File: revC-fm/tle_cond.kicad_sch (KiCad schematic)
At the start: 13 parts, among them U33 AD1585ARTZ-REEL7, U34 LT6004CMS8#PBF

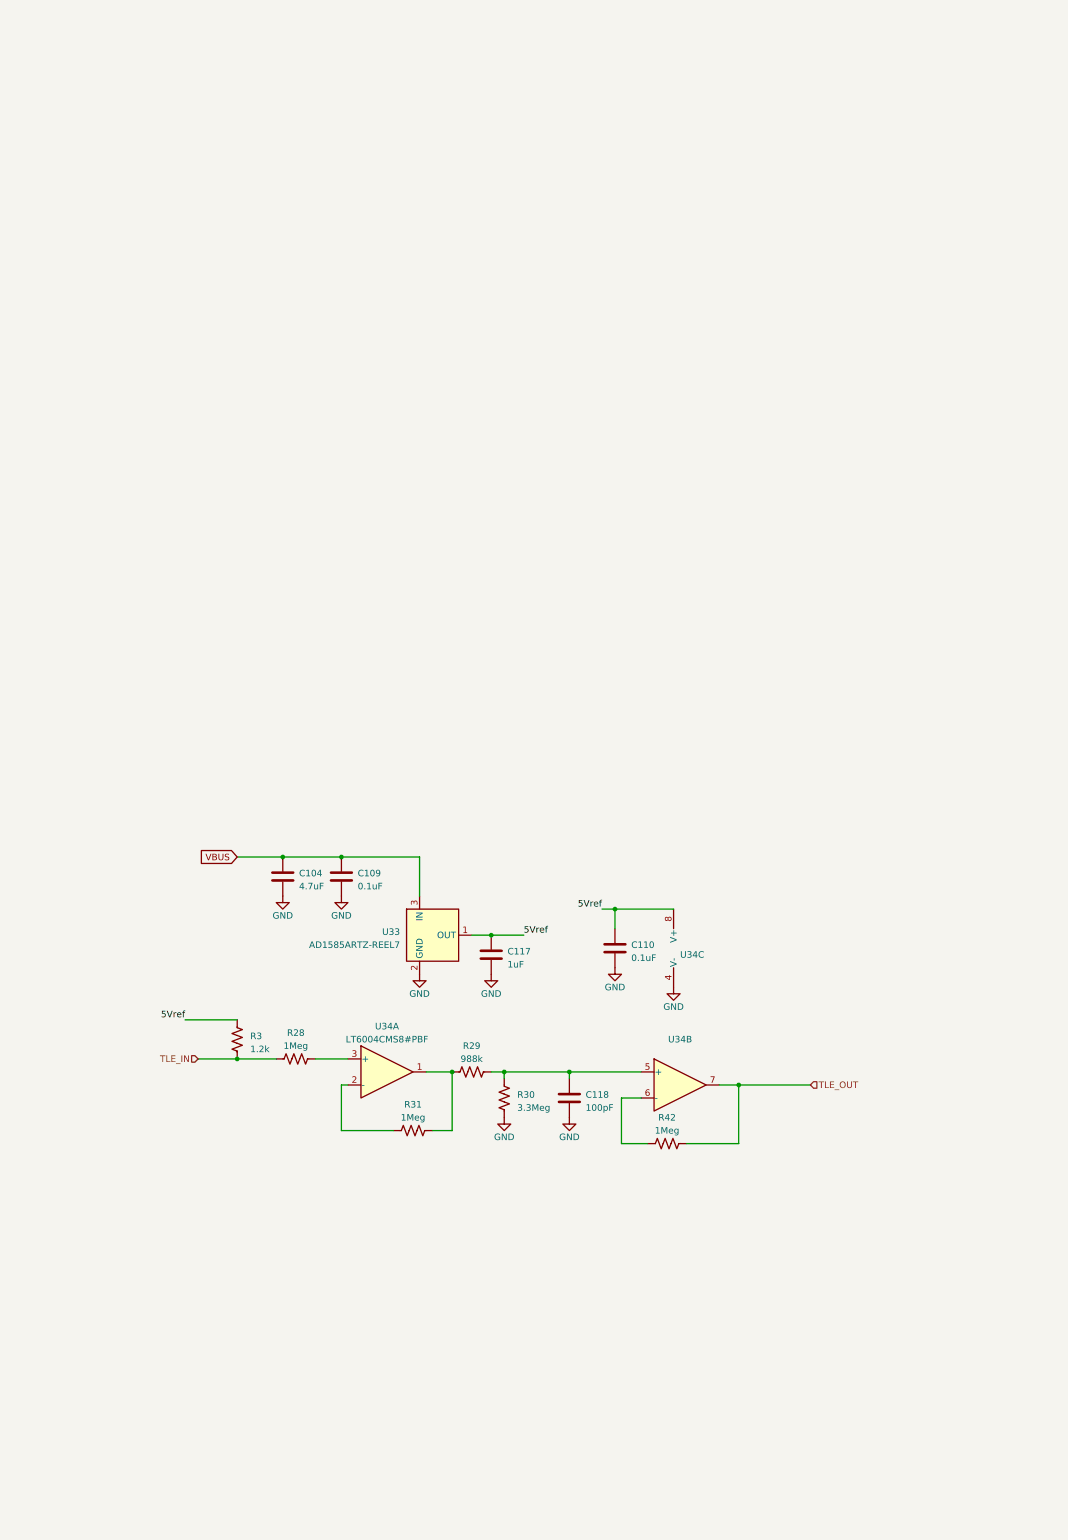
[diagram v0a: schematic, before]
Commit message: updated analog , solar comp, layout
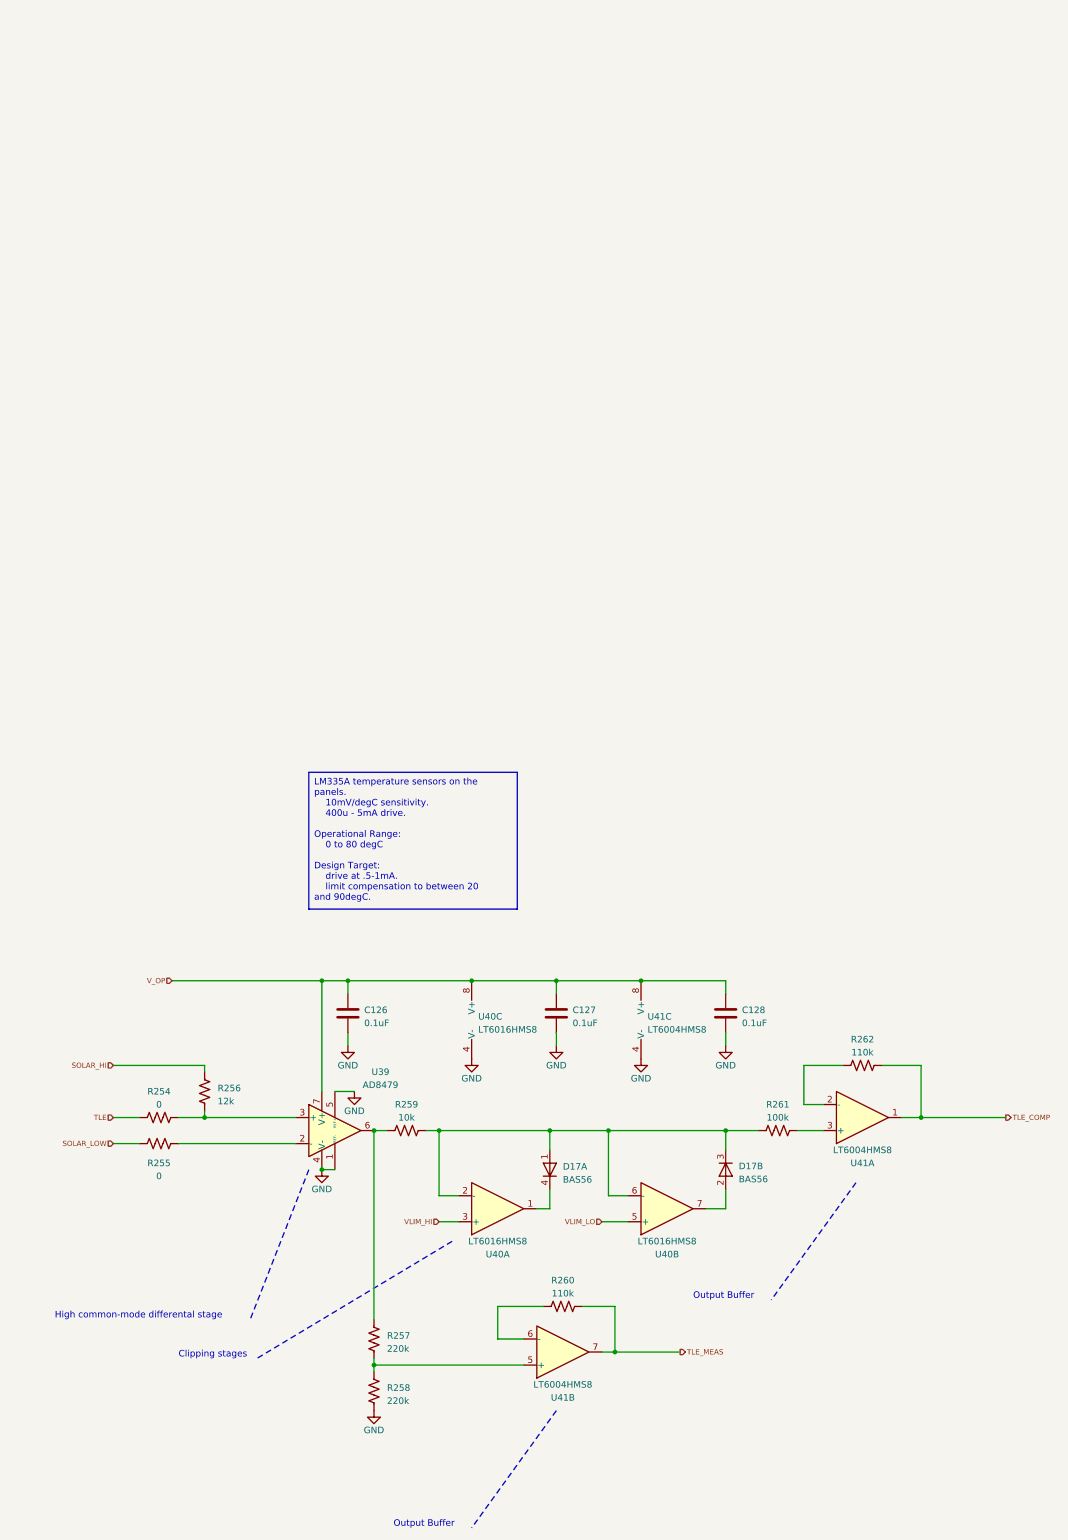
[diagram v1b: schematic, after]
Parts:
- removed C104: 4.7uF, Capacitor_SMD:C_0805_2012Metric, symbol Device:C
- removed C109, C110: 0.1uF, Capacitor_SMD:C_0603_1608Metric, symbol Device:C
- removed C117: 1uF, Capacitor_SMD:C_0603_1608Metric, symbol Device:C
- removed C118: 100pF, Capacitor_SMD:C_0603_1608Metric, symbol Device:C
- removed R28, R31, R42: 1Meg, Resistor_SMD:R_0603_1608Metric, symbol Device:R_US
- removed R29: 988k, Resistor_SMD:R_0603_1608Metric, symbol Device:R_US
- removed R3: 1.2k, Resistor_SMD:R_0805_2012Metric, symbol Device:R_US
- removed R30: 3.3Meg, Resistor_SMD:R_0603_1608Metric, symbol Device:R_US
- removed U33: AD1585ARTZ-REEL7, Package_TO_SOT_SMD:SOT-23-3, symbol SierraLobo:AD1585ARTZ-REEL7
- removed U34: LT6004CMS8#PBF, Package_SO:MSOP-8_3x3mm_P0.65mm, symbol SierraLobo:LT6004CMS8#PBF
- added C126, C127, C128: 0.1uF, Capacitor_SMD:C_0402_1005Metric, symbol Device:C
- added D17: BAS56, Package_TO_SOT_SMD:SOT-143, symbol SierraLobo:BAS56
- added R254, R255: 0, Resistor_SMD:R_0603_1608Metric, symbol Device:R_US
- added R256: 12k, Resistor_SMD:R_0805_2012Metric, symbol Device:R_US
- added R257, R258: 220k, Resistor_SMD:R_0603_1608Metric, symbol Device:R_US
- added R259: 10k, Resistor_SMD:R_0805_2012Metric, symbol Device:R_US
- added R260, R262: 110k, Resistor_SMD:R_0603_1608Metric, symbol Device:R_US
- added R261: 100k, Resistor_SMD:R_0603_1608Metric, symbol Device:R_US
- added U39: AD8479, Package_SO:SO-8_3.9x4.9mm_P1.27mm, symbol SierraLobo:AD8479
- added U40: LT6016HMS8, Package_SO:MSOP-8_3x3mm_P0.65mm, symbol SierraLobo:LT6016HMS8
- added U41: LT6004HMS8, Package_SO:MSOP-8_3x3mm_P0.65mm, symbol SierraLobo:LT6004HMS8
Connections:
- net GND: now also C126.2, C127.2, C128.2, R258.2, U39.1 (REF-), U39.4 (V-), U39.5 (REF+), U40.4 (V-), U41.4 (V-)
- new net: R257.1, R259.1, U39.6
- new net: D17.1 (K), D17.3 (A), R259.2, R261.1, U40.2 (-), U40.6 (-)
- new net: R260.1, U41.6 (-)
- new net: R262.1, U41.2 (-)
- new net: D17.2 (K), U40.7
- new net: R255.2, U39.2 (-)
- new net: D17.4 (A), U40.1
- new net: R257.2, R258.1, U41.5 (+)
- new net: R254.2, R256.2, U39.3 (+)
- new net: R261.2, U41.3 (+)
- new net SOLAR_HI: R256.1
- new net SOLAR_LOW: R255.1
- new net TLE: R254.1
- new net TLE_COMP: R262.2, U41.1
- new net TLE_MEAS: R260.2, U41.7
- new net VLIM_HI: U40.3 (+)
- new net VLIM_LO: U40.5 (+)
- new net V_OP: C126.1, C127.1, C128.1, U39.7 (V+), U40.8 (V+), U41.8 (V+)
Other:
- note added: "Clipping stages"
- note added: "High common-mode differental stage"
- note added: "Output Buffer"

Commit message: routing
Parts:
- C140: renamed from C126; footprint Capacitor_SMD:C_0402_1005Metric -> Capacitor_SMD:C_0603_1608Metric
- C141: renamed from C127; footprint Capacitor_SMD:C_0402_1005Metric -> Capacitor_SMD:C_0603_1608Metric
- C142: renamed from C128; footprint Capacitor_SMD:C_0402_1005Metric -> Capacitor_SMD:C_0603_1608Metric
- renumbered R262 to R247, R256 to R248, R254 to R249, R259 to R250, R261 to R251, R255 to R252, R260 to R253, R257 to R254, R258 to R255, U40 to U42, U41 to U43, U39 to U44

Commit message: changed RF connector to TH
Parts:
- renumbered C140 to C130, C141 to C131, C142 to C132, R247 to R243, R248 to R244, R249 to R245, R250 to R246, R251 to R247, R252 to R248, R253 to R249, R254 to R250, R255 to R251, U42 to U40, U43 to U41, U44 to U42

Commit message: working revC review changes
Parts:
- renumbered C130 to C131, C131 to C132, C132 to C133, D17 to D16, R243 to R260, R244 to R261, R245 to R262, R246 to R263, R247 to R264, R248 to R265, R249 to R266, R250 to R267, R251 to R268, U40 to U41, U41 to U42, U42 to U43

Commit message: working revC
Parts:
- removed C131, C133: 0.1uF, Capacitor_SMD:C_0603_1608Metric, symbol Device:C
- removed R265: 0, Resistor_SMD:R_0603_1608Metric, symbol Device:R_US
- removed unit 1 of U42
- removed unit 3 of U42
- removed U43: AD8479, Package_SO:SO-8_3.9x4.9mm_P1.27mm, symbol SierraLobo:AD8479
- added R305, R307, R309: R_US, symbol Device:R_US
- added U25: LT6004HMS8, Package_SO:MSOP-8_3x3mm_P0.65mm, symbol SierraLobo:LT6004HMS8
- added U49: ATL431BQ, Package_TO_SOT_SMD:SOT-23, symbol SierraLobo:ATL431BQ
- renumbered C132 to C74, D16 to D1, R260 to R75, R261 to R76, R262 to R77, R263 to R78, R264 to R79, R266 to R80, R267 to R81, R268 to R82, U41 to U20, U41 to U24, U42 to U26
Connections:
- net GND: now also R309.2, U25.2 (-), U49.3 (A)
- net TLE_COMP: now also U25.7
- net TLE_MEAS: now also U26.1; no longer U26.7
- net at R78.1, R81.1: now also U25.1
- net at R80.1: now also U26.2 (-); no longer U26.6 (-)
- net at R75.1: now also U25.5 (+)
- net at R81.2, R82.1: now also U26.3 (+); no longer U26.5 (+)
- net at R76.2, R77.2: now also U25.3 (+)
- net at R79.2: now also U25.6 (-)
- new net: R305.1, R307.1
- new net: R307.2, R309.1, U49.2 (REF)
- new net vref_hi: R305.2, U49.1 (K)
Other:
- note removed: "High common-mode differental stage"
- moved on the sheet: C74, D1A, D1B, R75, R76, R77, R78, R79, R80, R81, R82, U20A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
